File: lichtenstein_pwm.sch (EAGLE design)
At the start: 58 parts, among them IC1 LM2852Y-3V3, IC2 MCP23017, J1 MAGJACK, U1 ONION-OMEGA2

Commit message: Fixed some broken outputs; pwm output board added
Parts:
- removed C13: 47µF, rcl:CPOL-EUCT7343
- removed H2: MOUNT-HOLE2.8, holes:MOUNT-HOLE2.8
- removed R22, R23: 10k, rcl:R-EU_M0805
- added C14, C15: 100nF, rcl:C-EUC0805
- added IC3: (no value), lichtenstein_onion:AT24C02DSOIC-8
- added IC4: 74AHCT125SOIC14, lichtenstein_onion:74AHCT125SOIC14
- added SV5: 1792889, lichtenstein_onion:1792889
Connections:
- removed net INPUT6: IC2.PB4, R23.1, SV3.7
- removed net INPUT7: IC2.PB6, R22.1, SV3.9
- new net !PWM0_OE: IC2.PB7, IC4.!OE1
- new net !PWM1_OE: IC2.PB6, IC4.!OE2
- new net PWM0: IC4.A1, U1.PWM/G18
- new net PWM1: IC4.A2, U1.PWM/G19
- new net PWMOUT0: IC4.Y2, SV5.1
- new net PWMOUT1: IC4.Y1, SV5.3
- net +3V3: now also C14.2, IC3.A0, IC3.VCC, IC4.!OE3, IC4.!OE4; no longer C13.+, R22.2, R23.2
- net GND: now also C14.1, C15.1, IC3.A1, IC3.A2, IC3.GND, IC4.A3, IC4.A4, IC4.GND, SV5.2, SV5.4; no longer C13.-
- net I2C_SCL: now also IC3.SCL
- net I2C_SDA: now also IC3.SDA
- net INPUT3: now also IC2.PB4; no longer IC2.PB7
- net V+: now also C15.2, IC4.VCC

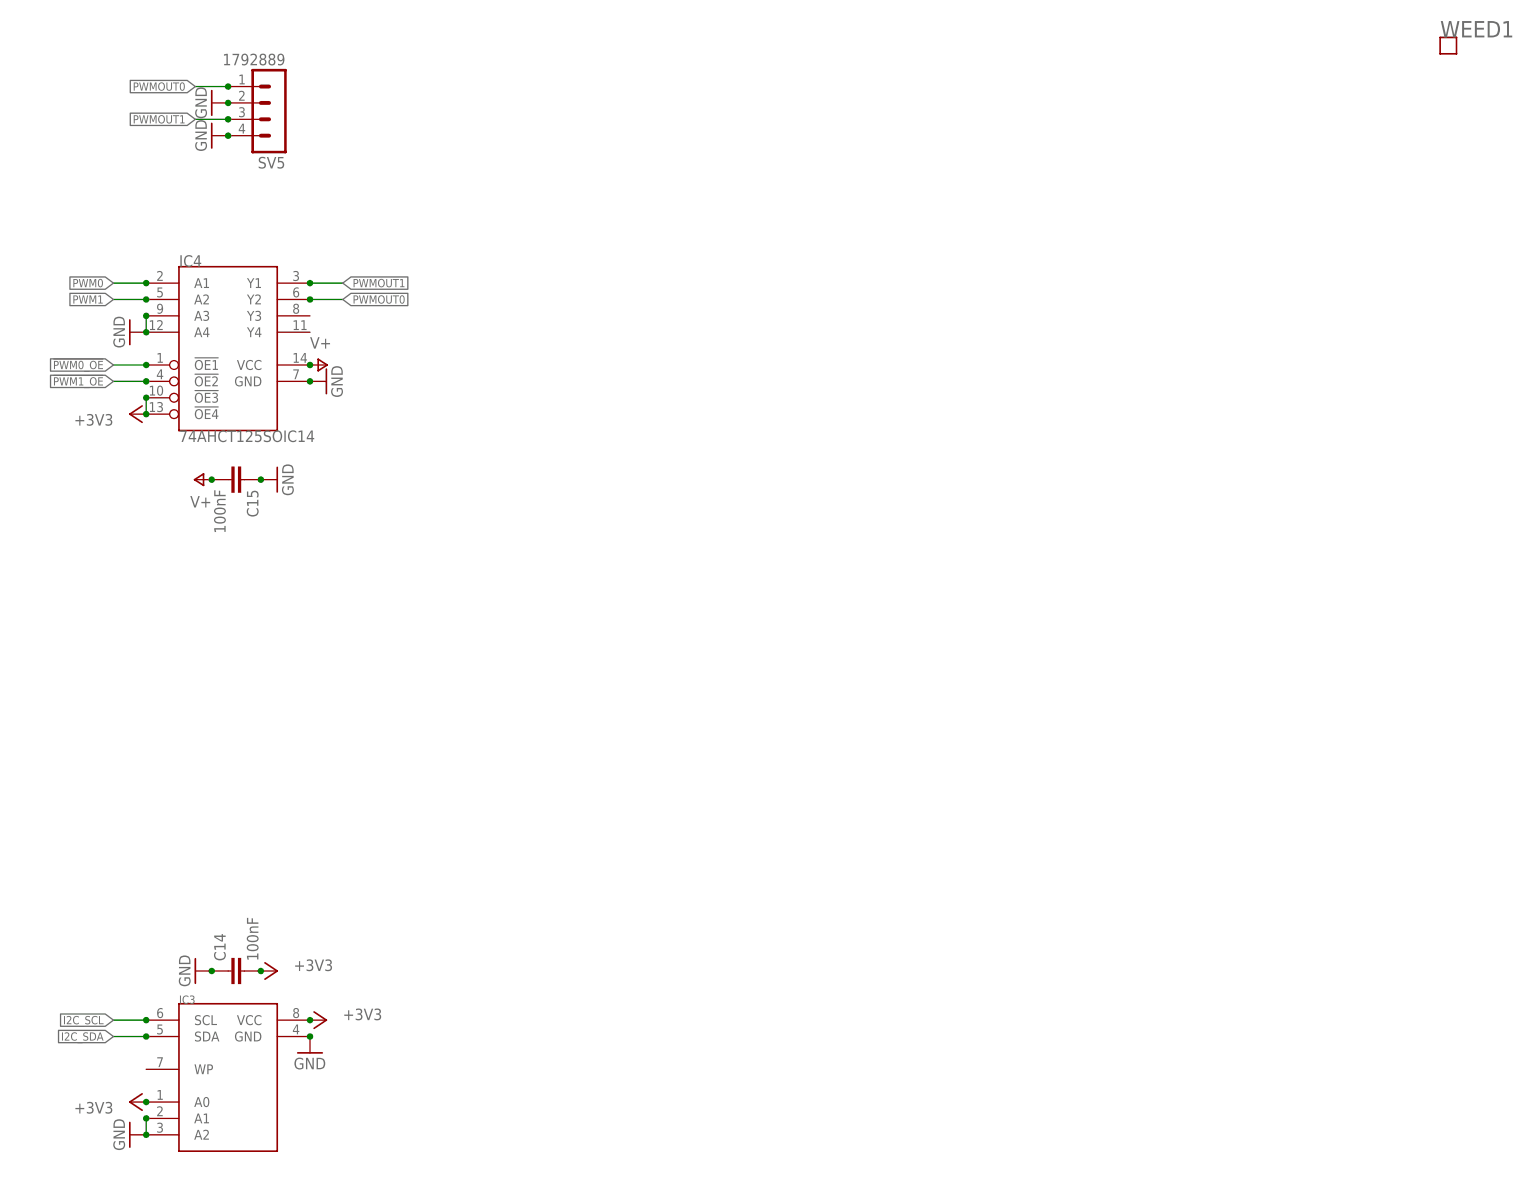
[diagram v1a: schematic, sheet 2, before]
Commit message: Cleaned up traces slightly for PWM board
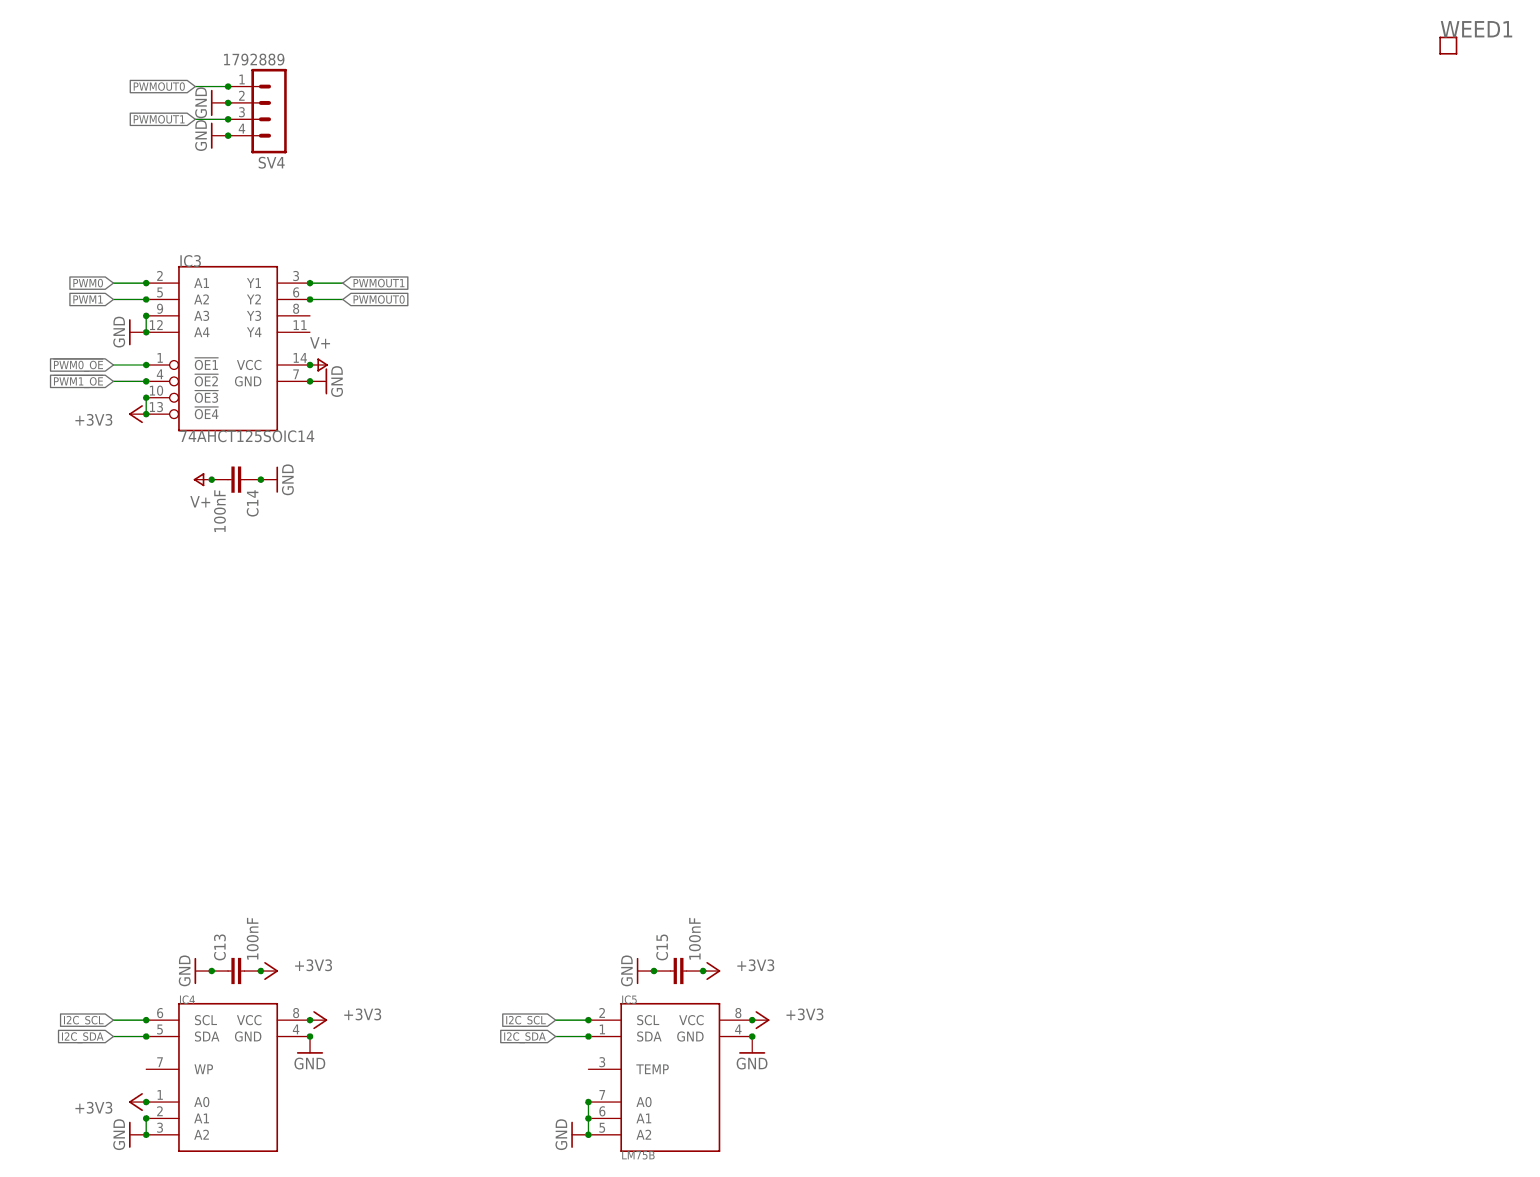
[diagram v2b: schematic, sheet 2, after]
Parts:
- removed H4: MOUNT-HOLE2.8, holes:MOUNT-HOLE2.8
- removed R24, R25: 10k, rcl:R-EU_M0805
- added C13: 100nF, rcl:C-EUC0805
- added H2: MOUNT-HOLE2.8, holes:MOUNT-HOLE2.8
- added IC5: LM75B, lichtenstein_onion:LM75B
- added R22, R23: 680R, rcl:R-EU_M0805
- IC3: value (none) -> 74AHCT125SOIC14; device lichtenstein_onion:AT24C02DSOIC-8 -> lichtenstein_onion:74AHCT125SOIC14
- IC4: value 74AHCT125SOIC14 -> (none); device lichtenstein_onion:74AHCT125SOIC14 -> lichtenstein_onion:AT24C02DSOIC-8
- R1: value 49.9R -> 10k; MOUSER 652-CR0805FX-49R9ELF -> 652-CR0805FX-1002ELF
- R11: value 49.9R -> 680R; MOUSER 652-CR0805FX-49R9ELF -> 652-CR0805-FX6800GLF
- R14: value 10k -> 680R; MOUSER 652-CR0805FX-1002ELF -> 652-CR0805-FX6800GLF
- R15: value 10k -> 49.9R; MOUSER 652-CR0805FX-1002ELF -> 652-CR0805FX-49R9ELF
- R2, R3: value 4k7 -> 10k; MOUSER 652-CR0805-FX4701GLF -> 652-CR0805FX-1002ELF
- R4: value 49.9R -> 10k; MOUSER 652-CR0805-FX4701GLF -> 652-CR0805FX-1002ELF
- R6, R7: value 680R -> 4k7; MOUSER 652-CR0805-FX6800GLF -> 652-CR0805-FX4701GLF
- R8: value 680R -> 49.9R; MOUSER 652-CR0805-FX6800GLF -> 652-CR0805-FX4701GLF
- R9: value 680R -> 49.9R; MOUSER 652-CR0805-FX6800GLF -> 652-CR0805FX-49R9ELF
- renumbered SV5 to SV4
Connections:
- new net !SPI_CS_1: U1.G16/U_TX2
- net !PWM0_OE: now also IC3.!OE1; no longer IC4.!OE1
- net !PWM1_OE: now also IC3.!OE2; no longer IC4.!OE2
- net +3V3: now also C13.2, C15.2, IC3.!OE3, IC3.!OE4, IC4.A0, IC4.VCC, IC5.VCC, R1.1, R16.2, R17.2, R2.1, R3.1, R4.1, R6.2, R7.2; no longer C14.2, IC3.A0, IC3.VCC, IC4.!OE3, IC4.!OE4, R10.1, R15.1, R16.1, R17.1, R2.2, R24.2, R25.2, R3.2
- net ETH_LED_ACT: now also R22.2; no longer R12.2
- net ETH_LED_LINK: now also R23.2; no longer R13.2
- net ETH_RX+: now also R9.1; no longer R5.1
- net ETH_RX-: now also R15.1; no longer R11.1
- net ETH_TX+: now also R5.1; no longer R1.1
- net ETH_TX-: now also R8.1; no longer R4.1
- net GND: now also C13.1, IC3.A3, IC3.A4, IC4.A1, IC4.A2, IC5.A0, IC5.A1, IC5.A2; no longer IC3.A1, IC3.A2, IC4.A3, IC4.A4
- net I2C_SCL: now also IC4.SCL, IC5.SCL, R7.1; no longer IC3.SCL, R3.1
- net I2C_SDA: now also IC4.SDA, IC5.SDA, R6.1; no longer IC3.SDA, R2.1
- net INPUT0: now also R16.1; no longer R18.1
- net INPUT1: now also R17.1; no longer R19.1
- net INPUT2: now also R20.1; no longer R24.1
- net INPUT3: now also R21.1; no longer R25.1
- net INPUT4: now also R18.1; no longer R20.1
- net INPUT5: now also R19.1; no longer R21.1
- net N$1: now also R14.2; no longer R10.2
- net N$10: now also R12.2; no longer R8.2
- net N$11: now also R13.2; no longer R9.2
- net N$2: now also R10.2; no longer R6.2
- net N$3: now also R5.2, R8.2; no longer R1.2, R4.2
- net N$4: now also R22.1; no longer R12.1
- net N$5: now also R23.1; no longer R13.1
- net N$6: now also R15.2, R9.2; no longer R11.2, R5.2
- net N$9: now also R11.2; no longer R7.2
- net PWM0: now also IC3.A1; no longer IC4.A1
- net PWM1: now also IC3.A2; no longer IC4.A2
- net PWMOUT0: now also IC3.Y2; no longer IC4.Y2
- net PWMOUT1: now also IC3.Y1; no longer IC4.Y1
- net STATUS0: now also R10.1; no longer R6.1
- net STATUS1: now also R11.1; no longer R7.1
- net STATUS2: now also R12.1; no longer R8.1
- net STATUS3: now also R13.1; no longer R9.1
- net TEST0: now also R1.2; no longer R17.2
- net TEST1: now also R2.2; no longer R16.2
- net TEST2: now also R3.2; no longer R15.2
- net TEST3: now also R4.2; no longer R14.2
- net V+: now also C14.2, IC3.VCC; no longer C15.2, IC4.VCC
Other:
- moved on the sheet: C14, C15, H3, R1, R10, R11, R12, R13, R14, R15, R16, R17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
